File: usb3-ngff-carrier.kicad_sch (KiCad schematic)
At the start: 63 parts, among them J1 KUSBX-BS1N9-1-BL30, J2 2199119-3, J3 Jack-DC, J5 Conn_01x03_Male, J6 SIM2070-6-1-30-00-A, J8 SIM2070-6-1-30-00-A, SW1 KMR221GLFS, U1 AP62301WU7

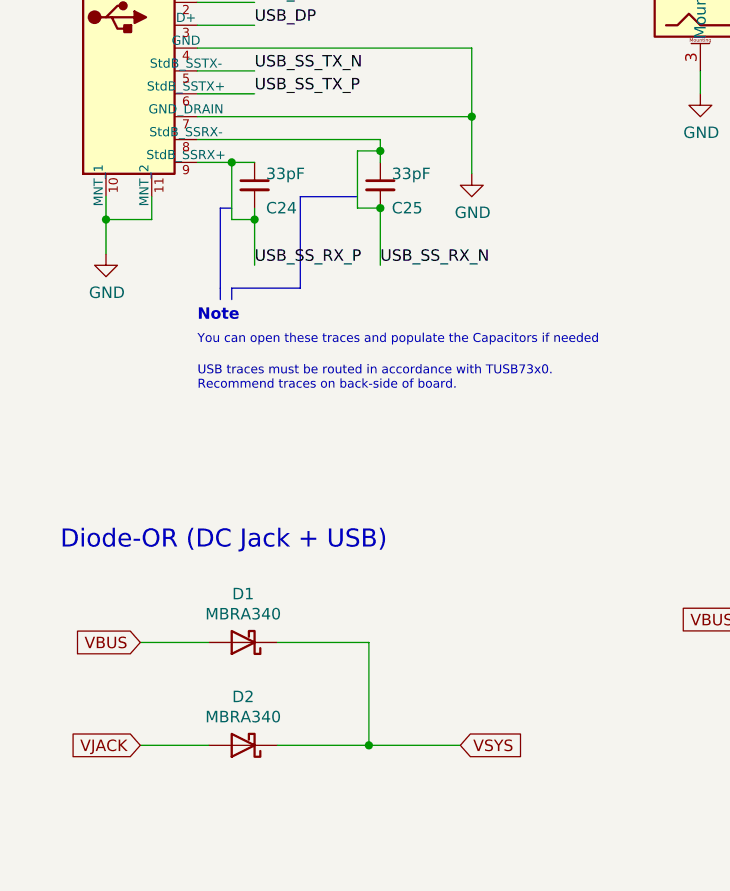
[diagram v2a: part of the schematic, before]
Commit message: fix: reduces optional USB Caps pads to 0402 and exposes a piece of their track
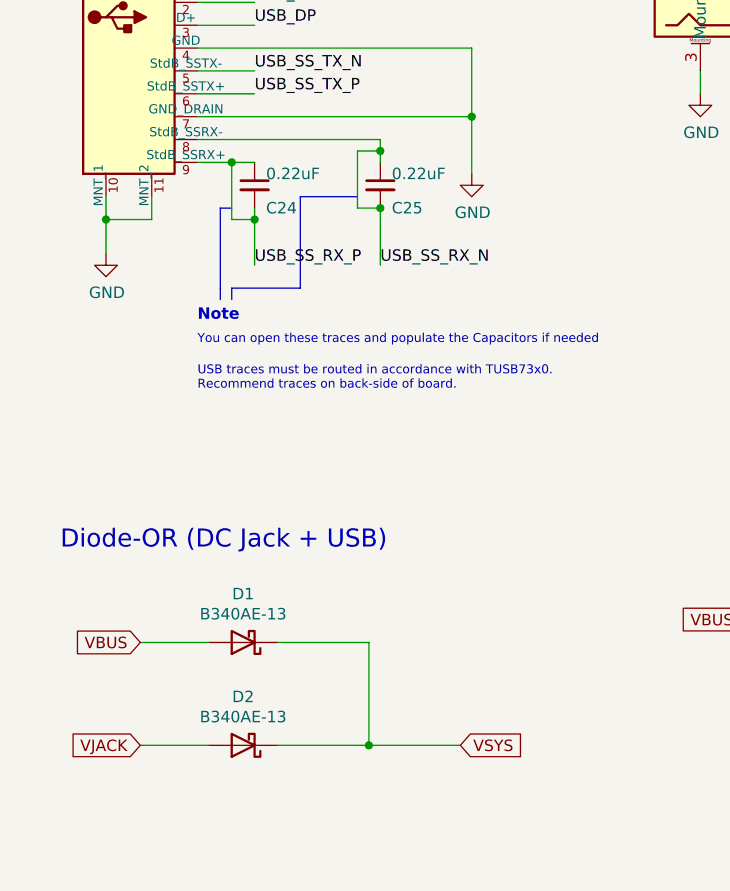
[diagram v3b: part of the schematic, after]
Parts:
- C24, C25: value 33pF -> 0.22uF; footprint Capacitor_SMD:C_0603_1608Metric -> Capacitor_SMD:C_0402_1005Metric_Pad0.74x0.62mm_HandSolder; MPN 06035A330KAT2A -> CGA2B3X7R1E224K050BB; Mfr AVX -> TDX; SKU 581-06035A330KAT2A -> (none)
- D1, D2: value MBRA340 -> B340AE-13; Int @ 10 0.262 -> (none); MPN MBRA340T3G -> B340AE-13; SKU 863-MBRA340T3G -> (none)
- H1, H2: Int @ 10 0.785 -> (none); MPN 9774015243R -> 9774020243R; SKU 710-9774015243R -> (none)
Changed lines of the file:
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@@
     (comment 4 "Damien Walsh 2020 - www.damow.net")
   )
-  (junction (at 73.66 73.66) (diameter 0) (color 0 0 0 0)
-  )
   (junction (at 339.09 53.34) (diameter 0) (color 0 0 0 0)
   )
@@
   (junction (at 339.09 72.39) (diameter 0) (color 0 0 0 0)
   )
+  (junction (at 73.66 73.66) (diameter 0) (color 0 0 0 0)
+  )
   (junction (at 114.3 171.45) (diameter 0) (color 0 0 0 0)
   )
@@
     (in_bom yes) (on_board yes)
     (property "Reference" "D1" (id 0) (at 58.42 116.5352 0))
-    (property "Value" "MBRA340" (id 1) (at 58.42 118.7704 0))
+    (property "Value" "B340AE-13" (id 1) (at 58.42 118.7704 0))
     (property "Footprint" "Diode_SMD:D_SMA" (id 2) (at 58.42 117.475 0)
       (effects (font (size 1.27 1.27)) hide)
     )
-    (property "Datasheet" "https://www.onsemi.com/pub/Collateral/MBRA340T3-D.PDF" (id 3) (at 58.42 121.92 0)
+    (property "Datasheet" "" (id 3) (at 58.42 121.92 0)
       (effects (font (size 1.27 1.27)) hide)
     )
-    (property "Int @ 10" "0.262" (id 4) (at 58.42 121.92 0)
+    (property "Int @ 10" "" (id 4) (at 58.42 121.92 0)
       (effects (font (size 1.27 1.27)) hide)
     )
-    (property "MPN" "MBRA340T3G" (id 5) (at 58.42 121.92 0)
+    (property "MPN" "B340AE-13" (id 5) (at 58.42 121.92 0)
       (effects (font (size 1.27 1.27)) hide)
     )
@@
       (effects (font (size 1.27 1.27)) hide)
     )
-    (property "SKU" "863-MBRA340T3G " (id 7) (at 58.42 121.92 0)
+    (property "SKU" "" (id 7) (at 58.42 121.92 0)
       (effects (font (size 1.27 1.27)) hide)
     )
@@
     (in_bom yes) (on_board yes)
     (property "Reference" "D2" (id 0) (at 58.42 127.9652 0))
-    (property "Value" "MBRA340" (id 1) (at 58.42 130.2004 0))
+    (property "Value" "B340AE-13" (id 1) (at 58.42 130.2004 0))
     (property "Footprint" "Diode_SMD:D_SMA" (id 2) (at 58.42 128.905 0)
       (effects (font (size 1.27 1.27)) hide)
     )
-    (property "Datasheet" "https://www.onsemi.com/pub/Collateral/MBRA340T3-D.PDF" (id 3) (at 58.42 133.35 0)
+    (property "Datasheet" "" (id 3) (at 58.42 133.35 0)
       (effects (font (size 1.27 1.27)) hide)
     )
-    (property "Int @ 10" "0.262" (id 4) (at 58.42 133.35 0)
+    (property "Int @ 10" "" (id 4) (at 58.42 133.35 0)
       (effects (font (size 1.27 1.27)) hide)
     )
-    (property "MPN" "MBRA340T3G" (id 5) (at 58.42 133.35 0)
+    (property "MPN" "B340AE-13" (id 5) (at 58.42 133.35 0)
       (effects (font (size 1.27 1.27)) hide)
     )
@@
       (effects (font (size 1.27 1.27)) hide)
     )
-    (property "SKU" "863-MBRA340T3G " (id 7) (at 58.42 133.35 0)
+    (property "SKU" "" (id 7) (at 58.42 133.35 0)
       (effects (font (size 1.27 1.27)) hide)
     )
@@
       (effects (font (size 1.27 1.27)) hide)
     )
-    (property "Datasheet" "https://www.mouser.co.uk/datasheet/2/445/9774015243R-1728818.pdf" (id 3) (at 127 254 0)
+    (property "Datasheet" "" (id 3) (at 127 254 0)
       (effects (font (size 1.27 1.27)) hide)
     )
-    (property "Int @ 10" "0.785" (id 4) (at 127 254 0)
+    (property "Int @ 10" "" (id 4) (at 127 254 0)
       (effects (font (size 1.27 1.27)) hide)
     )
-    (property "MPN" "9774015243R" (id 5) (at 127 254 0)
+    (property "MPN" "9774020243R" (id 5) (at 127 254 0)
       (effects (font (size 1.27 1.27)) hide)
     )
@@
       (effects (font (size 1.27 1.27)) hide)
     )
-    (property "SKU" "710-9774015243R" (id 7) (at 127 254 0)
+    (property "SKU" "" (id 7) (at 127 254 0)
       (effects (font (size 1.27 1.27)) hide)
     )
@@
       (effects (font (size 1.27 1.27)) hide)
     )
-    (property "Datasheet" "https://www.mouser.co.uk/datasheet/2/445/9774015243R-1728818.pdf" (id 3) (at 127 260.35 0)
+    (property "Datasheet" "" (id 3) (at 127 260.35 0)
       (effects (font (size 1.27 1.27)) hide)
     )
-    (property "Int @ 10" "0.785" (id 4) (at 127 260.35 0)
+    (property "Int @ 10" "" (id 4) (at 127 260.35 0)
       (effects (font (size 1.27 1.27)) hide)
     )
-    (property "MPN" "9774015243R" (id 5) (at 127 260.35 0)
+    (property "MPN" "9774020243R" (id 5) (at 127 260.35 0)
       (effects (font (size 1.27 1.27)) hide)
     )
@@
       (effects (font (size 1.27 1.27)) hide)
     )
-    (property "SKU" "710-9774015243R" (id 7) (at 127 260.35 0)
+    (property "SKU" "" (id 7) (at 127 260.35 0)
       (effects (font (size 1.27 1.27)) hide)
     )
@@
     (pin "2")
   )
-  (symbol (lib_id "Device:C_Small") (at 73.66 71.12 0) (unit 1)
-    (in_bom yes) (on_board yes)
-    (property "Reference" "C25" (id 0) (at 74.93 73.66 0)
-      (effects (font (size 1.27 1.27)) (justify left))
-    )
-    (property "Value" "33pF" (id 1) (at 74.93 69.85 0)
-      (effects (font (size 1.27 1.27)) (justify left))
-    )
-    (property "Footprint" "Capacitor_SMD:C_0603_1608Metric" (id 2) (at 74.6252 74.93 0)
-      (effects (font (size 1.27 1.27)) hide)
-    )
-    (property "Datasheet" "~" (id 3) (at 73.66 71.12 0)
-      (effects (font (size 1.27 1.27)) hide)
-    )
-    (property "Int @ 10" "0.023" (id 4) (at 73.66 71.12 0)
-      (effects (font (size 1.27 1.27)) hide)
-    )
-    (property "MPN" "06035A330KAT2A" (id 5) (at 73.66 71.12 0)
-      (effects (font (size 1.27 1.27)) hide)
-    )
-    (property "Mfr" "AVX" (id 6) (at 73.66 71.12 0)
-      (effects (font (size 1.27 1.27)) hide)
-    )
-    (property "SKU" "581-06035A330KAT2A" (id 7) (at 73.66 71.12 0)
-      (effects (font (size 1.27 1.27)) hide)
-    )
-    (property "Vendor" "Mouser" (id 8) (at 73.66 71.12 0)
-      (effects (font (size 1.27 1.27)) hide)
-    )
-    (pin "1")
-    (pin "2")
-  )
   (symbol (lib_id "Device:C_Small") (at 59.69 71.12 0) (unit 1)
     (in_bom yes) (on_board yes)
@@
       (effects (font (size 1.27 1.27)) (justify left))
     )
-    (property "Value" "33pF" (id 1) (at 60.96 69.85 0)
+    (property "Value" "0.22uF" (id 1) (at 60.96 69.85 0)
       (effects (font (size 1.27 1.27)) (justify left))
     )
-    (property "Footprint" "Capacitor_SMD:C_0603_1608Metric" (id 2) (at 60.6552 74.93 0)
+    (property "Footprint" "Capacitor_SMD:C_0402_1005Metric_Pad0.74x0.62mm_HandSolder" (id 2) (at 60.6552 74.93 0)
       (effects (font (size 1.27 1.27)) hide)
     )
@@
       (effects (font (size 1.27 1.27)) hide)
     )
-    (property "MPN" "06035A330KAT2A" (id 5) (at 59.69 71.12 0)
+    (property "MPN" "CGA2B3X7R1E224K050BB" (id 5) (at 59.69 71.12 0)
       (effects (font (size 1.27 1.27)) hide)
     )
-    (property "Mfr" "AVX" (id 6) (at 59.69 71.12 0)
+    (property "Mfr" "TDX" (id 6) (at 59.69 71.12 0)
       (effects (font (size 1.27 1.27)) hide)
     )
-    (property "SKU" "581-06035A330KAT2A" (id 7) (at 59.69 71.12 0)
+    (property "SKU" "" (id 7) (at 59.69 71.12 0)
       (effects (font (size 1.27 1.27)) hide)
     )
@@
     (pin "SW2")
   )
+  (symbol (lib_id "Device:C_Small") (at 73.66 71.12 0) (unit 1)
+    (in_bom yes) (on_board yes)
+    (property "Reference" "C25" (id 0) (at 74.93 73.66 0)
+      (effects (font (size 1.27 1.27)) (justify left))
+    )
+    (property "Value" "0.22uF" (id 1) (at 74.93 69.85 0)
+      (effects (font (size 1.27 1.27)) (justify left))
+    )
+    (property "Footprint" "Capacitor_SMD:C_0402_1005Metric_Pad0.74x0.62mm_HandSolder" (id 2) (at 74.6252 74.93 0)
+      (effects (font (size 1.27 1.27)) hide)
+    )
+    (property "Datasheet" "~" (id 3) (at 73.66 71.12 0)
+      (effects (font (size 1.27 1.27)) hide)
+    )
+    (property "Int @ 10" "0.023" (id 4) (at 73.66 71.12 0)
+      (effects (font (size 1.27 1.27)) hide)
+    )
+    (property "MPN" "CGA2B3X7R1E224K050BB" (id 5) (at 73.66 71.12 0)
+      (effects (font (size 1.27 1.27)) hide)
+    )
+    (property "Mfr" "TDX" (id 6) (at 73.66 71.12 0)
+      (effects (font (size 1.27 1.27)) hide)
+    )
+    (property "SKU" "" (id 7) (at 73.66 71.12 0)
+      (effects (font (size 1.27 1.27)) hide)
+    )
+    (property "Vendor" "Mouser" (id 8) (at 73.66 71.12 0)
+      (effects (font (size 1.27 1.27)) hide)
+    )
+    (pin "1")
+    (pin "2")
+  )
   (sheet_instances
     (path "/" (page "1"))
@@
     )
     (path "/3d3ecfd3-7034-4857-8323-70157dfe6123"
-      (reference "C24") (unit 1) (value "33pF") (footprint "Capacitor_SMD:C_0603_1608Metric")
+      (reference "C24") (unit 1) (value "0.22uF") (footprint "Capacitor_SMD:C_0402_1005Metric_Pad0.74x0.62mm_HandSolder")
     )
-    (path "/37a6db20-dae2-4e55-bf51-61d977d4126b"
-      (reference "C25") (unit 1) (value "33pF") (footprint "Capacitor_SMD:C_0603_1608Metric")
+    (path "/cf10b9f2-d4e8-4bc3-8a81-607dae800279"
+      (reference "C25") (unit 1) (value "0.22uF") (footprint "Capacitor_SMD:C_0402_1005Metric_Pad0.74x0.62mm_HandSolder")
     )
     (path "/00000000-0000-0000-0000-00005fb98a8c"
-      (reference "D1") (unit 1) (value "MBRA340") (footprint "Diode_SMD:D_SMA")
+      (reference "D1") (unit 1) (value "B340AE-13") (footprint "Diode_SMD:D_SMA")
     )
     (path "/00000000-0000-0000-0000-00005fc95bf1"
-      (reference "D2") (unit 1) (value "MBRA340") (footprint "Diode_SMD:D_SMA")
+      (reference "D2") (unit 1) (value "B340AE-13") (footprint "Diode_SMD:D_SMA")
     )
     (path "/00000000-0000-0000-0000-00005ff36d79"
